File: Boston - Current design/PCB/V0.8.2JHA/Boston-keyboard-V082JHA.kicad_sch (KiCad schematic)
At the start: 336 parts, among them J701 Conn_01x04_MountingPin, J702 Conn_01x03, J703 TYPE-C-31-M12_13, J706 Conn_ARM_JTAG_SWD_10, Q701 DTC123J, SW1 MXSwitch, SW10 MXSwitch, SW100 MXSwitch, SW101 MXSwitch, SW102 MXSwitch, SW103 MXSwitch, SW104 MXSwitch, SW105-1 MXSwitch, SW105-2 MXSwitch, SW106 MXSwitch, SW107 MXSwitch, SW108 MXSwitch, SW109 MXSwitch, SW11 MXSwitch, SW110 MXSwitch, SW111 MXSwitch, SW112 MXSwitch, SW113 MXSwitch, SW114 MXSwitch, SW115 MXSwitch, SW116 MXSwitch, SW117 MXSwitch, SW118 MXSwitch, SW119 MXSwitch, SW120 MXSwitch, SW121 MXSwitch, SW122 MXSwitch, SW123 MXSwitch, SW124-1 MXSwitch, SW124-2 MXSwitch, SW125 MXSwitch, SW126 Rotary_Encoder_Switch_Chassis, SW127 MXSwitch, SW128 MXSwitch, SW129 MXSwitch, SW13 MXSwitch, SW14 MXSwitch, SW15 MXSwitch, SW16 MXSwitch, SW17 MXSwitch, SW18 MXSwitch, SW19 MXSwitch, SW2 MXSwitch, SW20 MXSwitch, SW200 SW_Push, SW21 MXSwitch, SW22 MXSwitch, SW23 MXSwitch, SW24 MXSwitch, SW25 MXSwitch, SW26 MXSwitch, SW27 MXSwitch, SW28 MXSwitch, SW29 MXSwitch, SW3 MXSwitch, SW30 MXSwitch, SW31 MXSwitch, SW32 MXSwitch, SW33 MXSwitch, SW34 MXSwitch, SW35 MXSwitch, SW36 MXSwitch, SW37 MXSwitch, SW38 MXSwitch, SW39-1 MXSwitch, SW39-2 MXSwitch, SW4 MXSwitch, SW40 MXSwitch, SW41 MXSwitch, SW42 MXSwitch, SW43 MXSwitch, SW44 MXSwitch, SW45 MXSwitch, SW46 MXSwitch, SW47 MXSwitch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

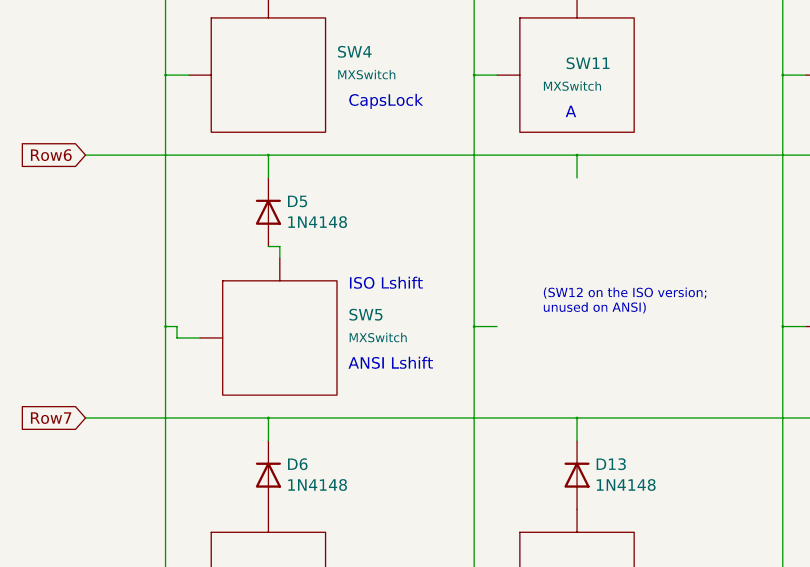
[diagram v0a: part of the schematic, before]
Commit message: Removed unused ISO left shift reference in the schematic
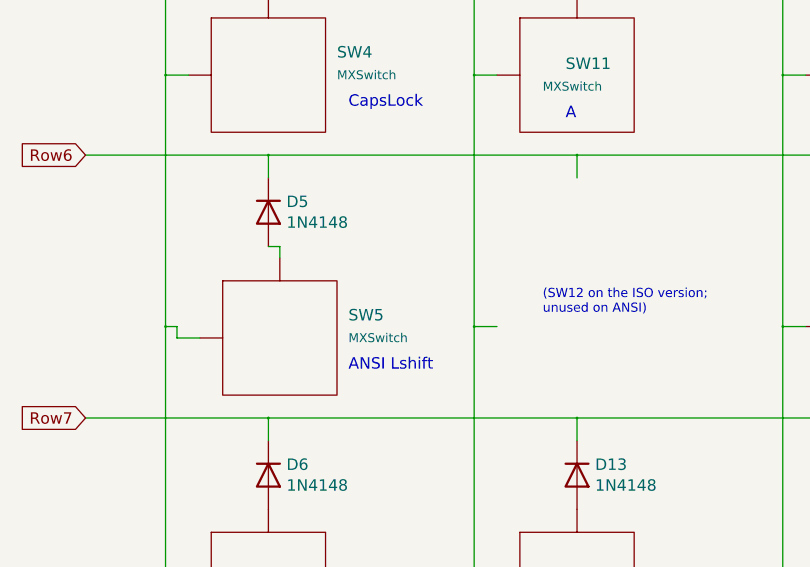
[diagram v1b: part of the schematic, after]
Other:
- note removed: "ISO Lshift"
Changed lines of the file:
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@@
-    (effects (font (size 1.27 1.27)) (justify left bottom))
-  )
-  (text "ISO Lshift\n" (at 54.61 200.66 0)
     (effects (font (size 1.27 1.27)) (justify left bottom))
   )

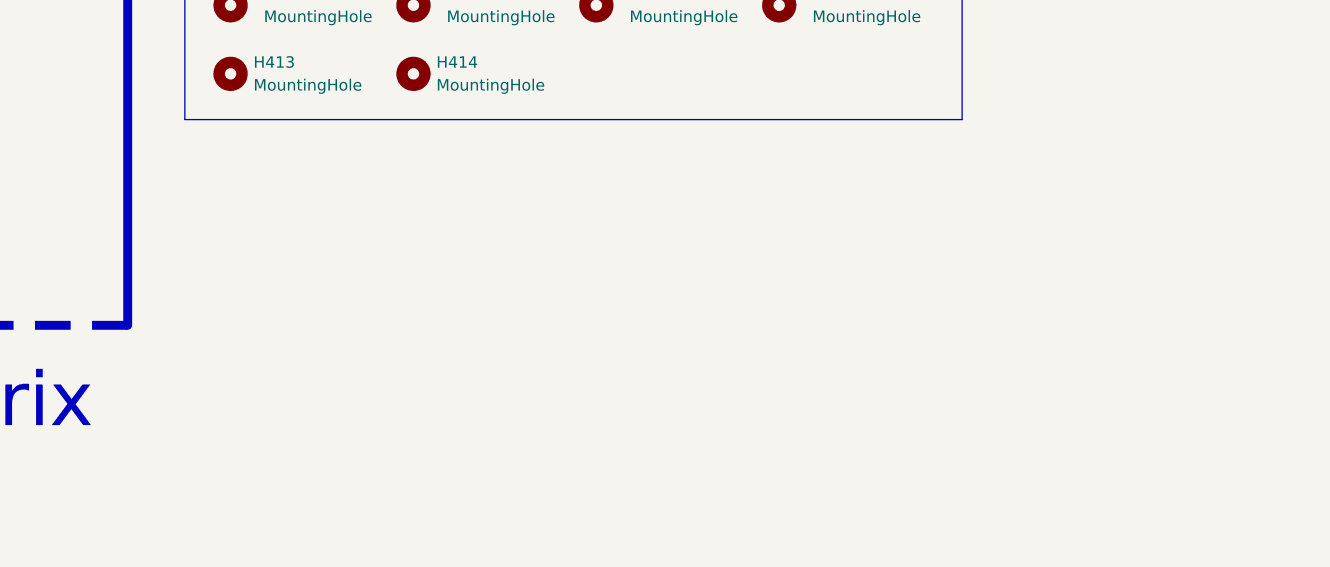
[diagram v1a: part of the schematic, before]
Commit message: Added note that SW123 and SW124-2 were accidentally swapped in the PCB layout
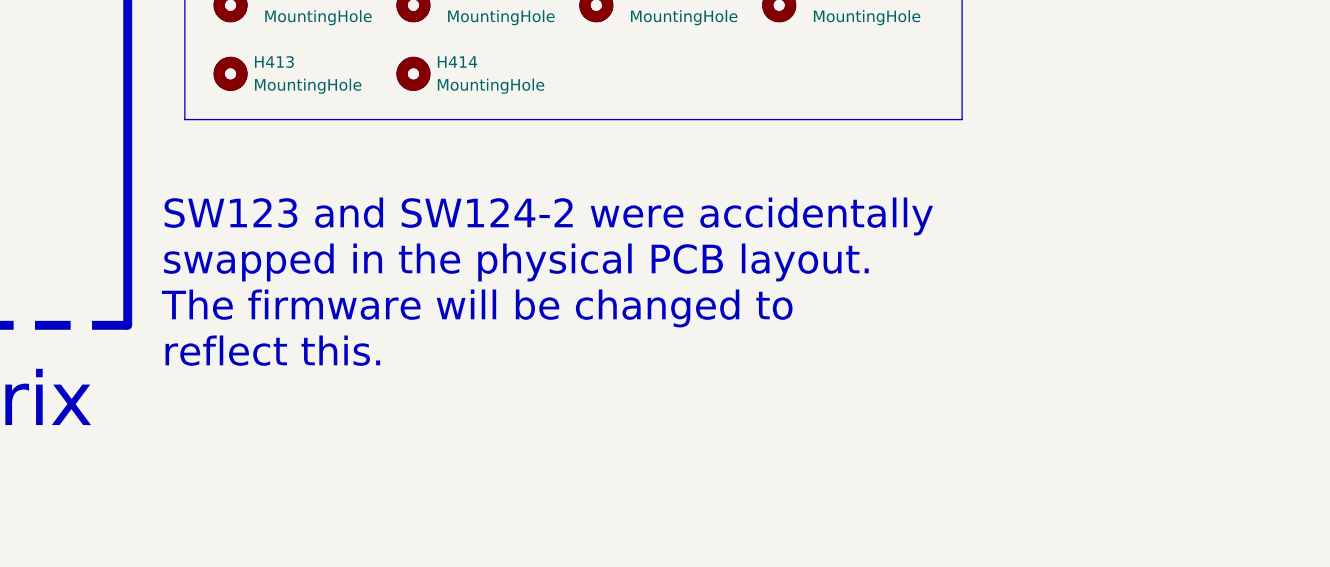
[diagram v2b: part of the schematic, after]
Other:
- note added: "SW123 and SW124-2 were accidentally swapped in the physical PCB layout. The firmware will be changed to reflect this."
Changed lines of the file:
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@@
     (effects (font (size 1.27 1.27)) (justify left bottom))
+  )
+  (text "SW123 and SW124-2 were accidentally \nswapped in the physical PCB layout. \nThe firmware will be changed to \nreflect this."
+    (at 694.69 259.08 0)
+    (effects (font (size 3.175 3.175)) (justify left bottom))
   )
   (text "Esc" (at 44.45 86.36 0)
